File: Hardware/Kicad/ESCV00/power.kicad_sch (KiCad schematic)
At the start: 53 parts, among them J1 FC, U1 INA181A3IDBVR, U2 LMR16006YDDCR, U3 MCP1703AT-3302E_MB

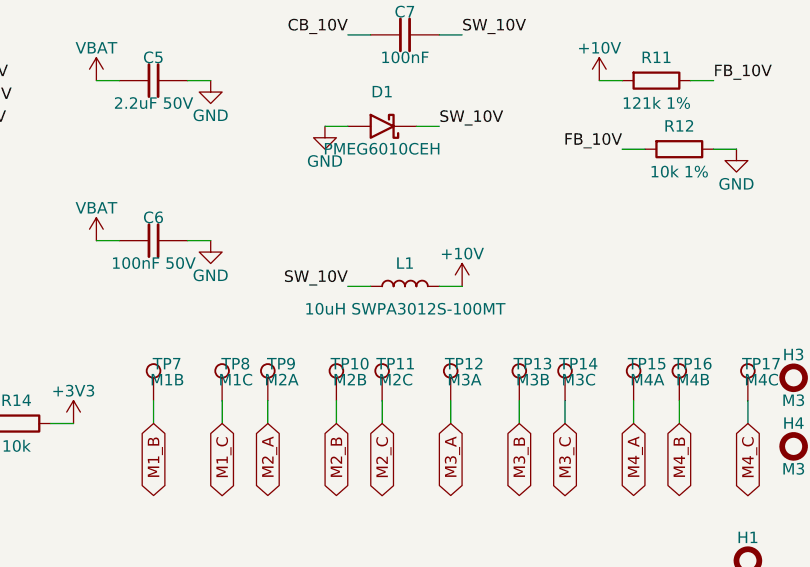
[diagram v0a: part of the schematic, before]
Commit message: Upgrade to KiCad 10 and use shared Kicad_Libs only
- Upgrade ESCV00, FCV00, RXV00, VTXV00 schematics and PCBs to KiCad 10
- Remove KiCad_Libs_Drone and merge_libs (parts already in Kicad_Libs)
- Lib tables list every Kicad_Libs library
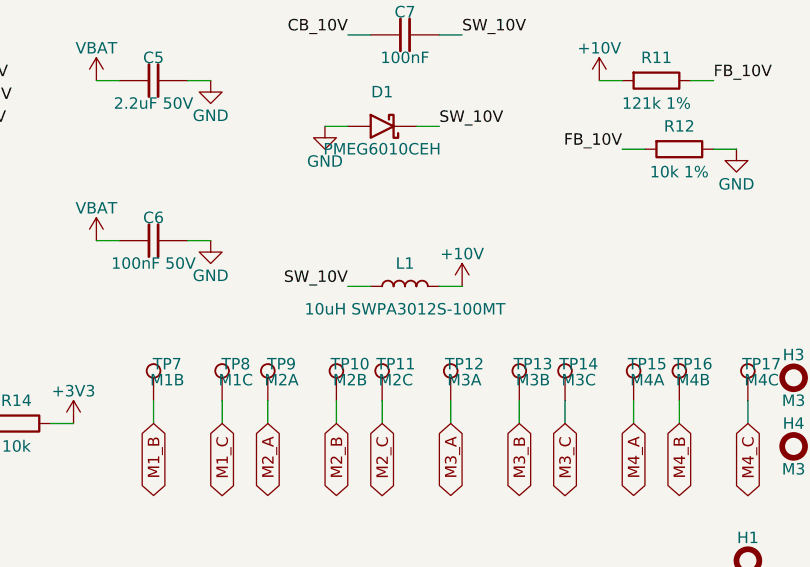
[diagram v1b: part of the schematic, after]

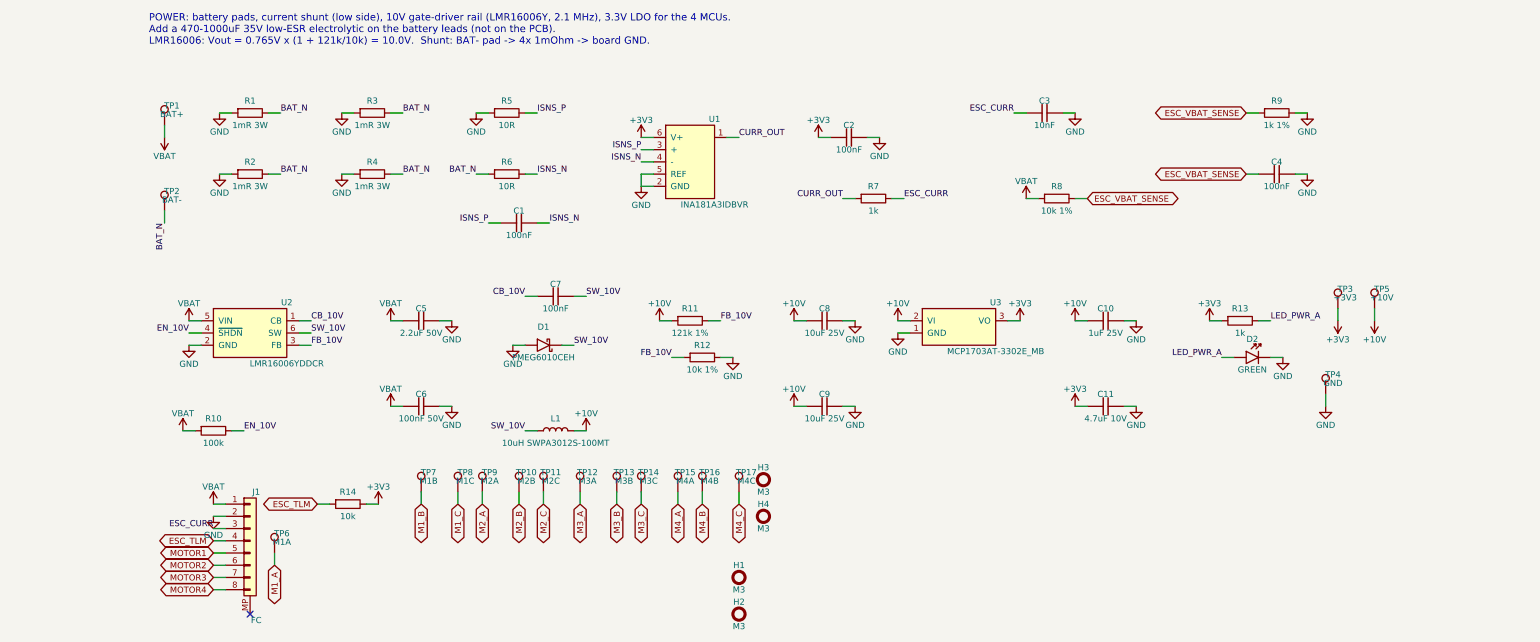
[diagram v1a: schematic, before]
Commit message: Boards follow the B0_EE part convention
- every real part uses the symbol/footprint/3D/datasheet named after its MPN in Kicad_Libs
- symbols keep only Reference, Value, Footprint, Datasheet, Description
  (MPN, Manufacturer, Verify, LCSC, Note fields removed; Verify notes moved to the Readme)
- schematic symbol caches rebuilt from the libraries, PCB footprints relinked with the
  same fields and 3D models as the library (connectivity unchanged)
- DNP and BOM attributes of the footprints match the symbols
- BOMs re-exported with kicad-cli
- ignore KiCad local history
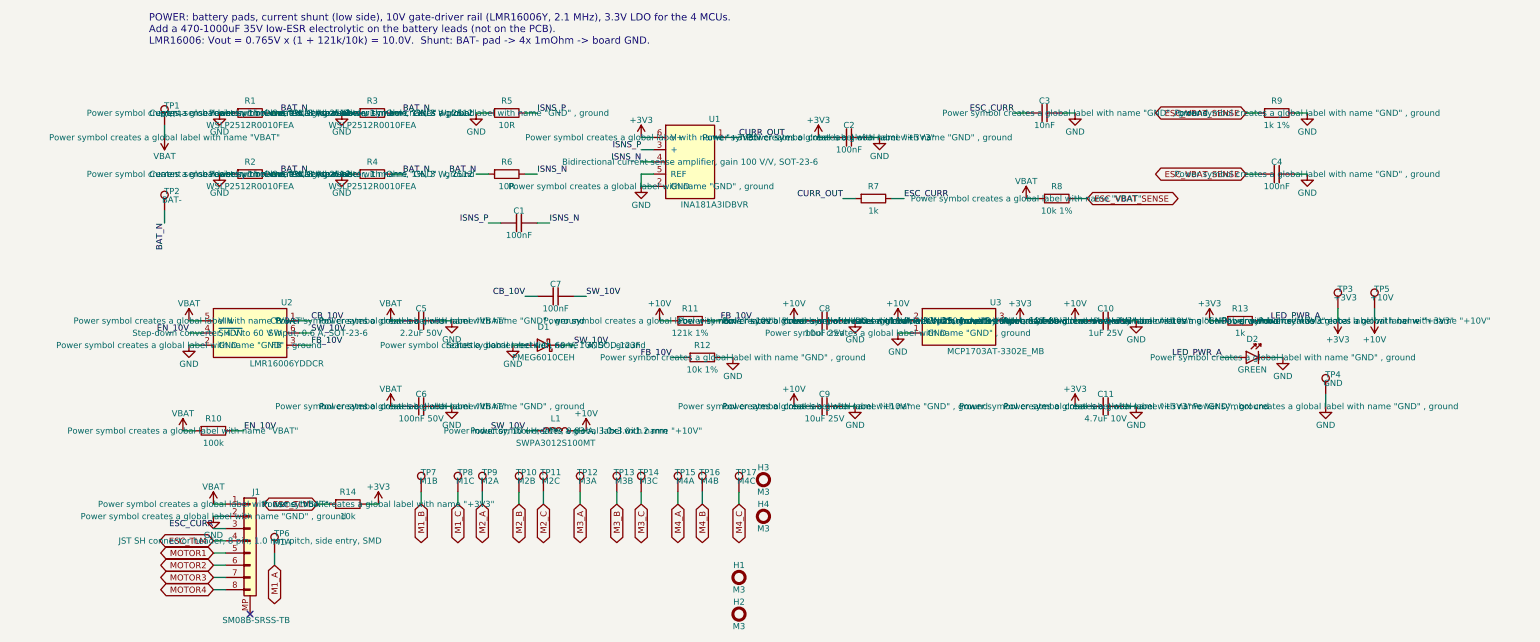
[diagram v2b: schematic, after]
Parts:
- D1: footprint eDiodes:D_SOD-123F -> eDiodes:PMEG6010CEH; symbol eDiodes:D_Schottky -> eDiodes:PMEG6010CEH; MPN PMEG6010CEH,115 -> (none)
- H1, H2, H3, H4, TP1, TP10, TP11, TP12, TP13, TP14, TP15, TP16, TP17, TP2, TP3, TP4, TP5, TP6, TP7, TP8, TP9: now left out of the parts list
- J1: value FC -> SM08B-SRSS-TB; footprint eConnector:JST_SH_SM08B-SRSS-TB_1x08-1MP_P1.00mm_Horizontal -> eConnector:SM08B-SRSS-TB; symbol eConnector:JST_SH_SM08B-SRSS-TB -> eConnector:SM08B-SRSS-TB; MPN SM08B-SRSS-TB(LF)(SN) -> (none); Manufacturer JST -> (none)
- L1: value 10uH SWPA3012S-100MT -> SWPA3012S100MT; footprint eCoil:L_Sunlord_SWPA3012S -> eCoil:SWPA3012S100MT; symbol eCoil:L -> eCoil:SWPA3012S100MT; MPN SWPA3012S100MT -> (none); Manufacturer Sunlord -> (none)
- R1, R2, R3, R4: value 1mR 3W -> WSLP2512R0010FEA; footprint eResistor:R_2512_6332Metric -> eResistor:WSLP2512R0010FEA; symbol eResistor:R -> eResistor:WSLP2512R0010FEA; MPN WSLP2512R0010FEA -> (none); Manufacturer Vishay -> (none)
- U1: footprint eAmplifier:SOT-23-6 -> eAmplifier:INA181A3IDBVR; MPN INA181A3IDBVR -> (none); Manufacturer Texas Instruments -> (none)
- U2: footprint eConverterDCDC:SOT-23-6 -> eConverterDCDC:LMR16006YDDCR; MPN LMR16006YDDCR -> (none); Manufacturer Texas Instruments -> (none)
- U3: footprint eLinearReg:SOT-89-3 -> eLinearReg:MCP1703AT-3302E_MB; MPN MCP1703AT-3302E/MB -> (none); Manufacturer Microchip -> (none)

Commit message: Cleared all the descriptions and started Power section for FCV
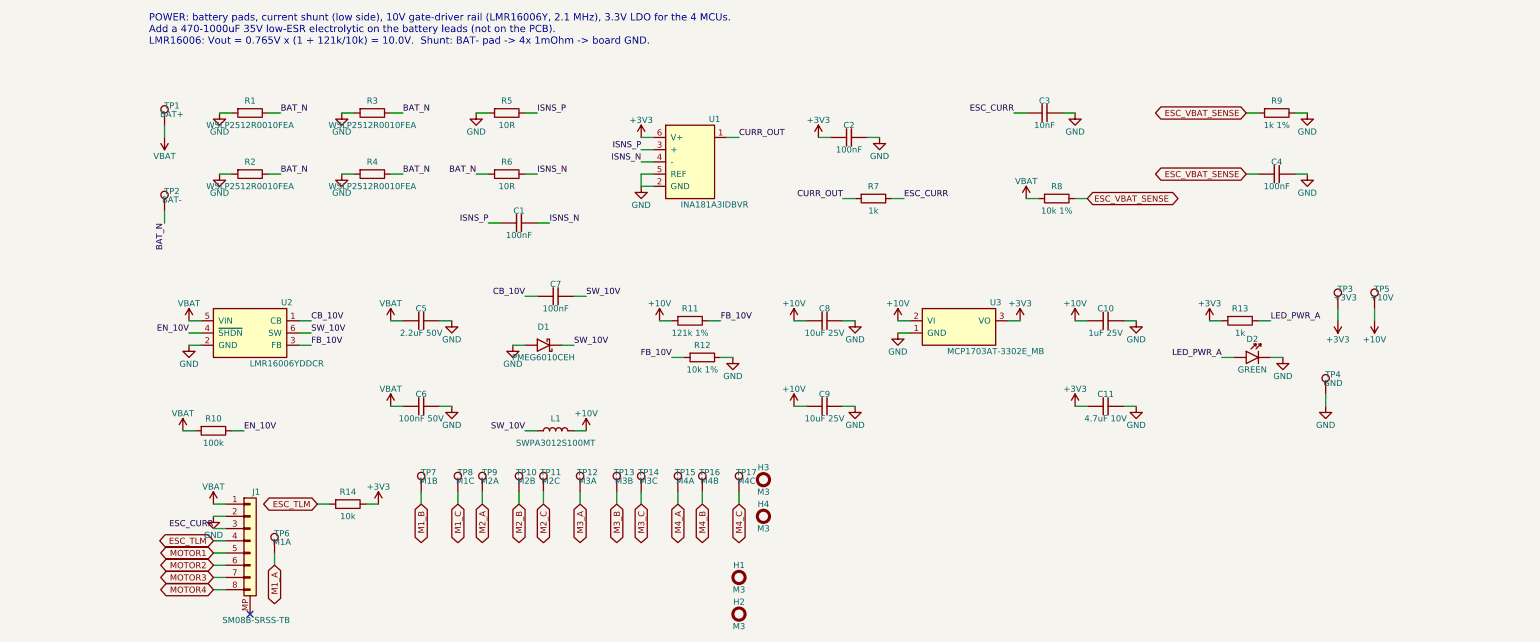
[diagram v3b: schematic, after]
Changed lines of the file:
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@@
 			(show_name no)
 			(do_not_autoplace no)
+			(hide yes)
 			(effects
 				(font
@@
 			(show_name no)
 			(do_not_autoplace no)
+			(hide yes)
 			(effects
 				(font
@@
 			(show_name no)
 			(do_not_autoplace no)
+			(hide yes)
 			(effects
 				(font
@@
 			(show_name no)
 			(do_not_autoplace no)
+			(hide yes)
 			(effects
 				(font
@@
 			(show_name no)
 			(do_not_autoplace no)
+			(hide yes)
 			(effects
 				(font
@@
 			(show_name no)
 			(do_not_autoplace no)
+			(hide yes)
 			(effects
 				(font
@@
 			(show_name no)
 			(do_not_autoplace no)
+			(hide yes)
 			(effects
 				(font
@@
 			(show_name no)
 			(do_not_autoplace no)
+			(hide yes)
 			(effects
 				(font
@@
 			(show_name no)
 			(do_not_autoplace no)
+			(hide yes)
 			(effects
 				(font
@@
 			(show_name no)
 			(do_not_autoplace no)
+			(hide yes)
 			(effects
 				(font
@@
 			(show_name no)
 			(do_not_autoplace no)
+			(hide yes)
 			(effects
 				(font
@@
 			(show_name no)
 			(do_not_autoplace no)
+			(hide yes)
 			(effects
 				(font
@@
 			(show_name no)
 			(do_not_autoplace no)
+			(hide yes)
 			(effects
 				(font
@@
 			(show_name no)
 			(do_not_autoplace no)
+			(hide yes)
 			(effects
 				(font
@@
 			(show_name no)
 			(do_not_autoplace no)
+			(hide yes)
 			(effects
 				(font
@@
 			(show_name no)
 			(do_not_autoplace no)
+			(hide yes)
 			(effects
 				(font
@@
 			(show_name no)
 			(do_not_autoplace no)
+			(hide yes)
 			(effects
 				(font
@@
 			(show_name no)
 			(do_not_autoplace no)
+			(hide yes)
 			(effects
 				(font
@@
 			(show_name no)
 			(do_not_autoplace no)
+			(hide yes)
 			(effects
 				(font
@@
 			(show_name no)
 			(do_not_autoplace no)
+			(hide yes)
 			(effects
 				(font
@@
 			(show_name no)
 			(do_not_autoplace no)
+			(hide yes)
 			(effects
 				(font
@@
 			(show_name no)
 			(do_not_autoplace no)
+			(hide yes)
 			(effects
 				(font
@@
 			(show_name no)
 			(do_not_autoplace no)
+			(hide yes)
 			(effects
 				(font
@@
 			(show_name no)
 			(do_not_autoplace no)
+			(hide yes)
 			(effects
 				(font
@@
 			(show_name no)
 			(do_not_autoplace no)
+			(hide yes)
 			(effects
 				(font
@@
 			(show_name no)
 			(do_not_autoplace no)
+			(hide yes)
 			(effects
 				(font
@@
 			(show_name no)
 			(do_not_autoplace no)
+			(hide yes)
 			(effects
 				(font
@@
 			(show_name no)
 			(do_not_autoplace no)
+			(hide yes)
 			(effects
 				(font
@@
 			(show_name no)
 			(do_not_autoplace no)
+			(hide yes)
 			(effects
 				(font
@@
 			(show_name no)
 			(do_not_autoplace no)
+			(hide yes)
 			(effects
 				(font
@@
 			(show_name no)
 			(do_not_autoplace no)
+			(hide yes)
 			(effects
 				(font
@@
 			(show_name no)
 			(do_not_autoplace no)
+			(hide yes)
 			(effects
 				(font
@@
 			(show_name no)
 			(do_not_autoplace no)
+			(hide yes)
 			(effects
 				(font
@@
 			(show_name no)
 			(do_not_autoplace no)
+			(hide yes)
 			(effects
 				(font
@@
 			(show_name no)
 			(do_not_autoplace no)
+			(hide yes)
 			(effects
 				(font
@@
 			(show_name no)
 			(do_not_autoplace no)
+			(hide yes)
 			(effects
 				(font
@@
 			(show_name no)
 			(do_not_autoplace no)
+			(hide yes)
 			(effects
 				(font
@@
 			(show_name no)
 			(do_not_autoplace no)
+			(hide yes)
 			(effects
 				(font
@@
 			(show_name no)
 			(do_not_autoplace no)
+			(hide yes)
 			(effects
 				(font
@@
 			(show_name no)
 			(do_not_autoplace no)
+			(hide yes)
 			(effects
 				(font
@@
 			(show_name no)
 			(do_not_autoplace no)
+			(hide yes)
 			(effects
 				(font
@@
 			(show_name no)
 			(do_not_autoplace no)
+			(hide yes)
 			(effects
 				(font
@@
 			(show_name no)
 			(do_not_autoplace no)
+			(hide yes)
 			(effects
 				(font
@@
 			(show_name no)
 			(do_not_autoplace no)
+			(hide yes)
 			(effects
 				(font
@@
 			(show_name no)
 			(do_not_autoplace no)
+			(hide yes)
 			(effects
 				(font
@@
 			(show_name no)
 			(do_not_autoplace no)
+			(hide yes)
 			(effects
 				(font
@@
 			(show_name no)
 			(do_not_autoplace no)
+			(hide yes)
 			(effects
 				(font
@@
 			(show_name no)
 			(do_not_autoplace no)
+			(hide yes)
 			(effects
 				(font
@@
 			(show_name no)
 			(do_not_autoplace no)
+			(hide yes)
 			(effects
 				(font
@@
 			(show_name no)
 			(do_not_autoplace no)
+			(hide yes)
 			(effects
 				(font
@@
 			(show_name no)
 			(do_not_autoplace no)
+			(hide yes)
 			(effects
 				(font
@@
 			(show_name no)
 			(do_not_autoplace no)
+			(hide yes)
 			(effects
 				(font
@@
 			(show_name no)
 			(do_not_autoplace no)
+			(hide yes)
 			(effects
 				(font
@@
 			(show_name no)
 			(do_not_autoplace no)
+			(hide yes)
 			(effects
 				(font
